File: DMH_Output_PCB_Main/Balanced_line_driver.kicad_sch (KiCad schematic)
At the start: 40 parts, among them J31 Conn_01x06_PinHeader, J32 Conn_01x06_PinHeader, U10 NE5532, U9 NE5532

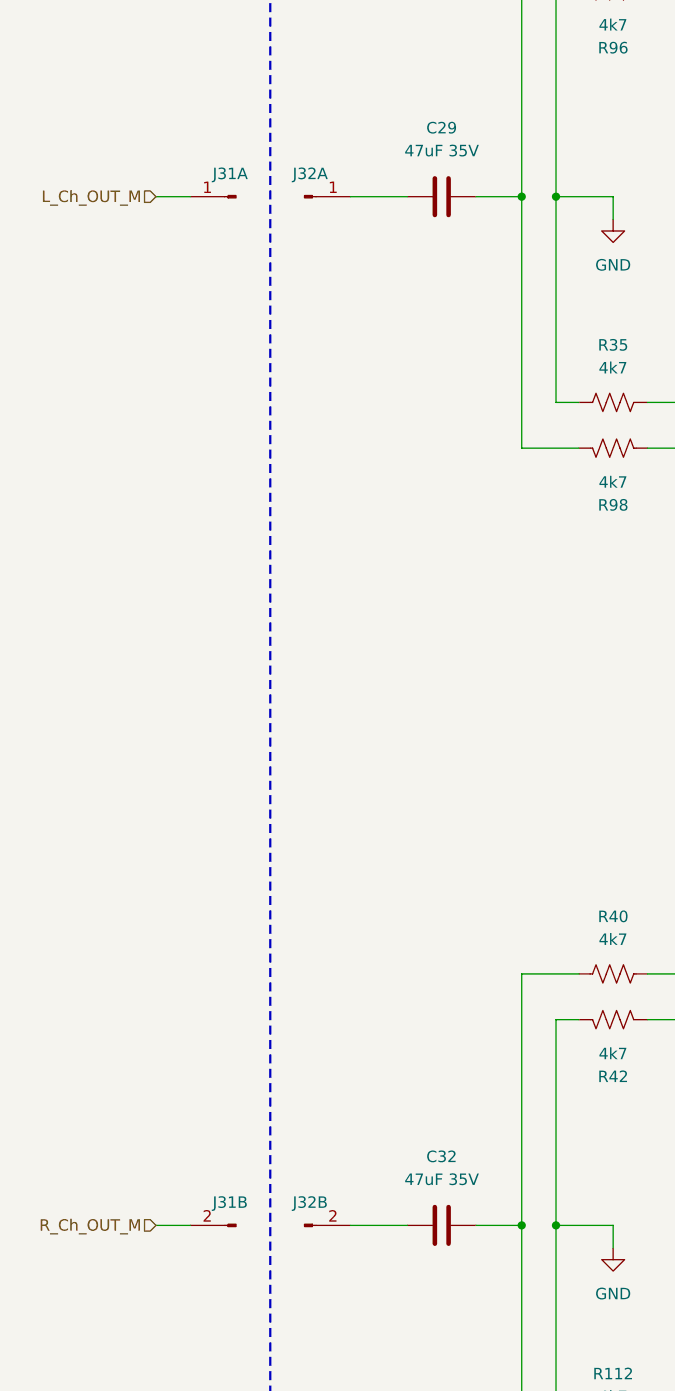
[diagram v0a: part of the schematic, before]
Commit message: Placed pin sockets
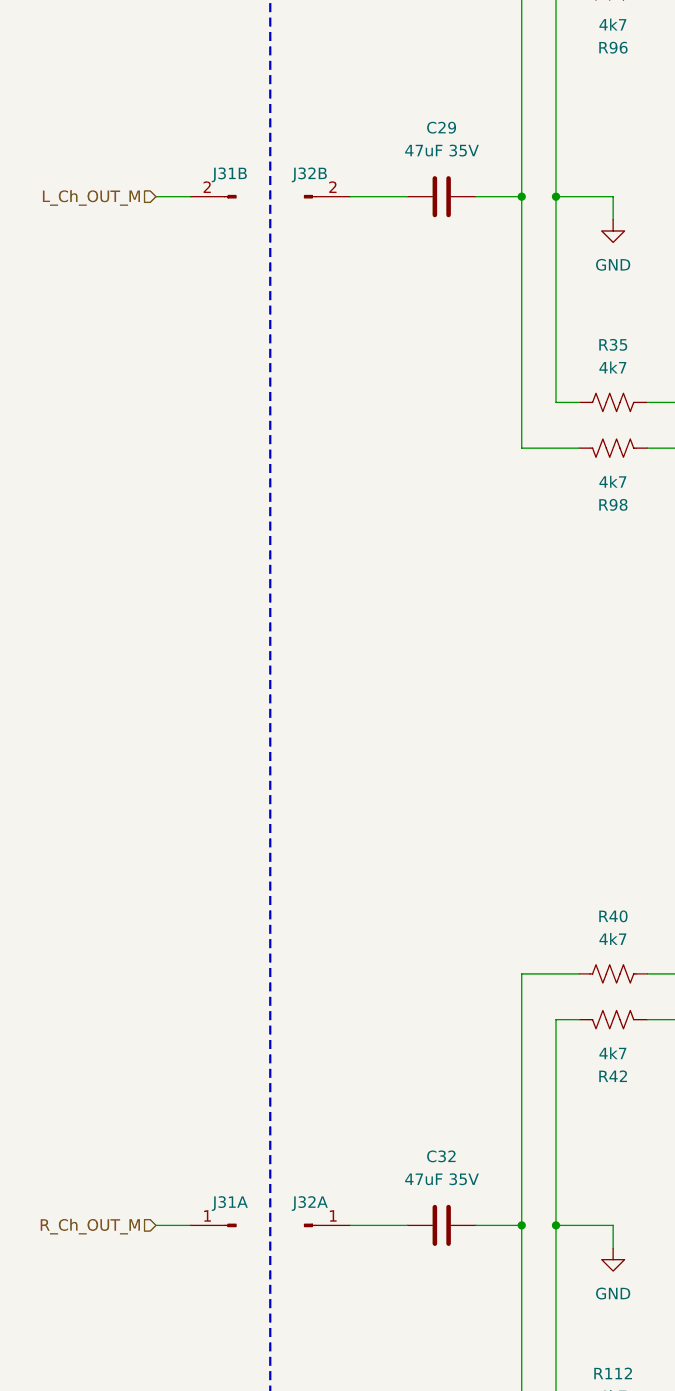
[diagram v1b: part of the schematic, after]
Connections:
- net L_Ch_OUT_M: now also J31.2 (Pin_2); no longer J31.1 (Pin_1)
- net R_Ch_OUT_M: now also J31.1 (Pin_1); no longer J31.2 (Pin_2)
- net at J32.2 (Pin_2): now also C29.1; no longer C32.1
- net at J32.1 (Pin_1): now also C32.1; no longer C29.1
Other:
- moved on the sheet: J31A, J31B, J32A, J32B
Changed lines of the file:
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@@
 	(symbol
 		(lib_id "SynthStuff:Conn_01x06_PinHeader")
-		(at 48.26 190.5 0)
+		(at 48.26 76.2 0)
 		(unit 2)
 		(body_style 1)
@@
 		(fields_autoplaced yes)
 		(property "Reference" "J32"
-			(at 48.895 187.96 0)
+			(at 48.895 73.66 0)
 			(show_name no)
 			(do_not_autoplace no)
@@
 		)
 		(property "Value" "Conn_01x06_PinHeader"
-			(at 48.26 193.04 0)
+			(at 48.26 78.74 0)
 			(hide yes)
 			(show_name no)
@@
 		)
 		(property "Footprint" "Connector_PinHeader_2.54mm:PinHeader_1x06_P2.54mm_Vertical"
-			(at 48.26 190.5 0)
-			(hide yes)
-			(show_name no)
-			(do_not_autoplace no)
-			(effects
-				(font
-					(size 1.27 1.27)
-				)
-			)
-		)
-		(property "Datasheet" ""
-			(at 48.26 190.5 0)
+			(at 48.26 76.2 0)
+			(hide yes)
+			(show_name no)
+			(do_not_autoplace no)
+			(effects
+				(font
+					(size 1.27 1.27)
+				)
+			)
+		)
+		(property "Datasheet" ""
+			(at 48.26 76.2 0)
 			(hide yes)
 			(show_name no)
@@
 		)
 		(property "Description" "Generic connector, single row, 01x06"
-			(at 48.26 190.5 0)
+			(at 48.26 76.2 0)
 			(hide yes)
 			(show_name no)
@@
 	(symbol
 		(lib_id "SynthStuff:Conn_01x06_PinHeader")
-		(at 40.64 190.5 180)
+		(at 40.64 76.2 180)
 		(unit 2)
 		(body_style 1)
@@
 		(fields_autoplaced yes)
 		(property "Reference" "J31"
-			(at 40.005 187.96 0)
+			(at 40.005 73.66 0)
 			(show_name no)
 			(do_not_autoplace no)
@@
 		)
 		(property "Value" "Conn_01x06_PinHeader"
-			(at 40.64 187.96 0)
+			(at 40.64 73.66 0)
 			(hide yes)
 			(show_name no)
@@
 		)
 		(property "Footprint" "Connector_PinSocket_2.54mm:PinSocket_1x06_P2.54mm_Vertical"
-			(at 40.64 190.5 0)
-			(hide yes)
-			(show_name no)
-			(do_not_autoplace no)
-			(effects
-				(font
-					(size 1.27 1.27)
-				)
-			)
-		)
-		(property "Datasheet" ""
-			(at 40.64 190.5 0)
+			(at 40.64 76.2 0)
+			(hide yes)
+			(show_name no)
+			(do_not_autoplace no)
+			(effects
+				(font
+					(size 1.27 1.27)
+				)
+			)
+		)
+		(property "Datasheet" ""
+			(at 40.64 76.2 0)
 			(hide yes)
 			(show_name no)
@@
 		)
 		(property "Description" "Generic connector, single row, 01x06"
-			(at 40.64 190.5 0)
+			(at 40.64 76.2 0)
 			(hide yes)
 			(show_name no)
@@
 	(symbol
 		(lib_id "SynthStuff:Conn_01x06_PinHeader")
-		(at 40.64 76.2 180)
+		(at 40.64 190.5 180)
 		(unit 1)
 		(body_style 1)
@@
 		(fields_autoplaced yes)
 		(property "Reference" "J31"
-			(at 40.005 73.66 0)
+			(at 40.005 187.96 0)
 			(show_name no)
 			(do_not_autoplace no)
@@
 		)
 		(property "Value" "Conn_01x06_PinHeader"
-			(at 40.64 73.66 0)
+			(at 40.64 187.96 0)
 			(hide yes)
 			(show_name no)
@@
 		)
 		(property "Footprint" "Connector_PinSocket_2.54mm:PinSocket_1x06_P2.54mm_Vertical"
-			(at 40.64 76.2 0)
-			(hide yes)
-			(show_name no)
-			(do_not_autoplace no)
-			(effects
-				(font
-					(size 1.27 1.27)
-				)
-			)
-		)
-		(property "Datasheet" ""
-			(at 40.64 76.2 0)
+			(at 40.64 190.5 0)
+			(hide yes)
+			(show_name no)
+			(do_not_autoplace no)
+			(effects
+				(font
+					(size 1.27 1.27)
+				)
+			)
+		)
+		(property "Datasheet" ""
+			(at 40.64 190.5 0)
 			(hide yes)
 			(show_name no)
@@
 		)
 		(property "Description" "Generic connector, single row, 01x06"
-			(at 40.64 76.2 0)
+			(at 40.64 190.5 0)
 			(hide yes)
 			(show_name no)
@@
 	(symbol
 		(lib_id "SynthStuff:Conn_01x06_PinHeader")
-		(at 48.26 76.2 0)
+		(at 48.26 190.5 0)
 		(unit 1)
 		(body_style 1)
@@
 		(fields_autoplaced yes)
 		(property "Reference" "J32"
-			(at 48.895 73.66 0)
+			(at 48.895 187.96 0)
 			(show_name no)
 			(do_not_autoplace no)
@@
 		)
 		(property "Value" "Conn_01x06_PinHeader"
-			(at 48.26 78.74 0)
+			(at 48.26 193.04 0)
 			(hide yes)
 			(show_name no)
@@
 		)
 		(property "Footprint" "Connector_PinHeader_2.54mm:PinHeader_1x06_P2.54mm_Vertical"
-			(at 48.26 76.2 0)
-			(hide yes)
-			(show_name no)
-			(do_not_autoplace no)
-			(effects
-				(font
-					(size 1.27 1.27)
-				)
-			)
-		)
-		(property "Datasheet" ""
-			(at 48.26 76.2 0)
+			(at 48.26 190.5 0)
+			(hide yes)
+			(show_name no)
+			(do_not_autoplace no)
+			(effects
+				(font
+					(size 1.27 1.27)
+				)
+			)
+		)
+		(property "Datasheet" ""
+			(at 48.26 190.5 0)
 			(hide yes)
 			(show_name no)
@@
 		)
 		(property "Description" "Generic connector, single row, 01x06"
-			(at 48.26 76.2 0)
-			(hide yes)
-			(show_name no)
+			(at 48.26 190.5 0)
+			(hide yes)
+			(show_name no)
